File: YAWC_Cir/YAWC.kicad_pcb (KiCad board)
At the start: 2 copper layers, 65 x 36.4 mm, 30 parts, among them P1 JST-PH_2, P2 Btns, P3 CONN_5, P4 CONN_5, P5 CONN_6, U1 TPS769XX, U2 SAMD20J18A-M, U3 MMA845Q

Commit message: Mount holes
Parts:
- added X: SolderWirePad_single_2mmDrill, Wire_Pads:SolderWirePad_single_2mmDrill, F.Cu at (128.0, 95.2)
- added X: SolderWirePad_single_2mmDrill, Wire_Pads:SolderWirePad_single_2mmDrill, F.Cu at (150.6, 113.4)
- added X: SolderWirePad_single_2mmDrill, Wire_Pads:SolderWirePad_single_2mmDrill, F.Cu at (182.9, 92.2)
- moved R2 2.20 mm to (177.9, 92.0)
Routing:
- net VCC: track 195.9 -> 193.2 mm
- net SDA: track 38.6 -> 36.3 mm

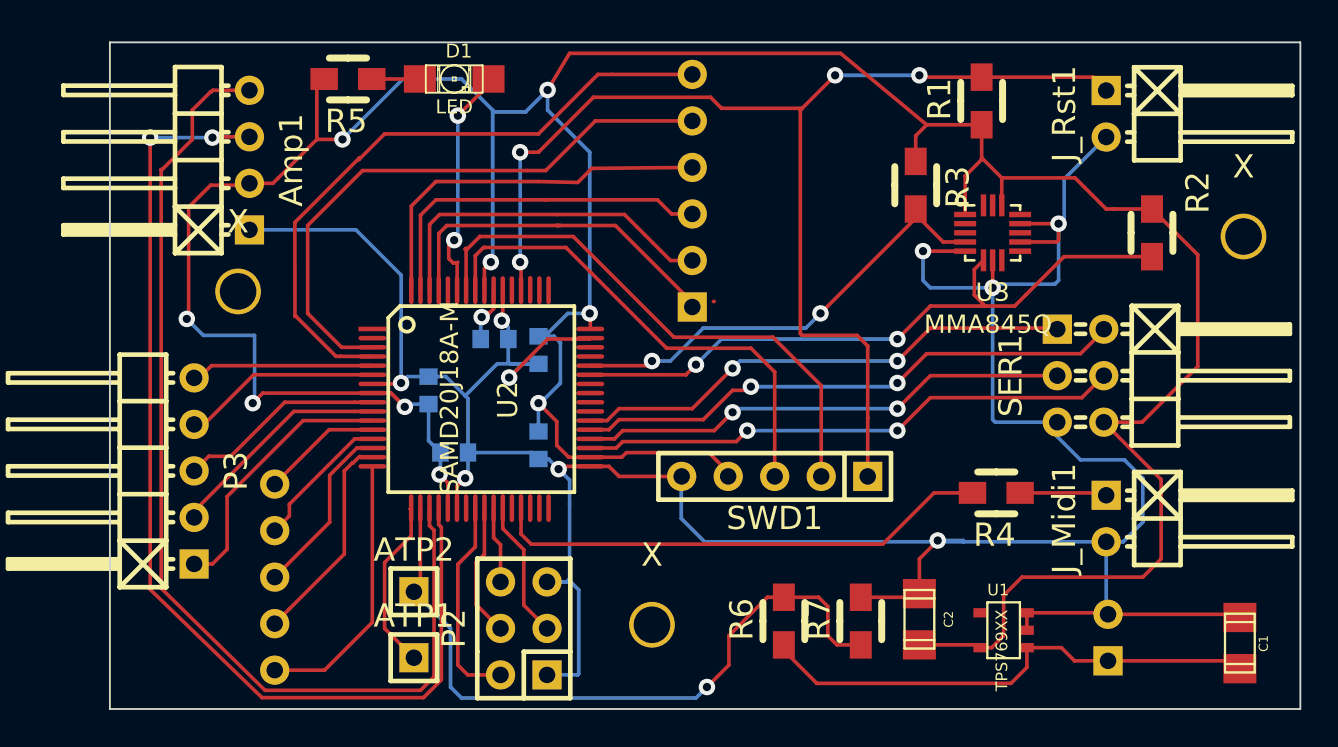
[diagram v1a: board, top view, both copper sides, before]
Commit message: Added fill Still need silk screen
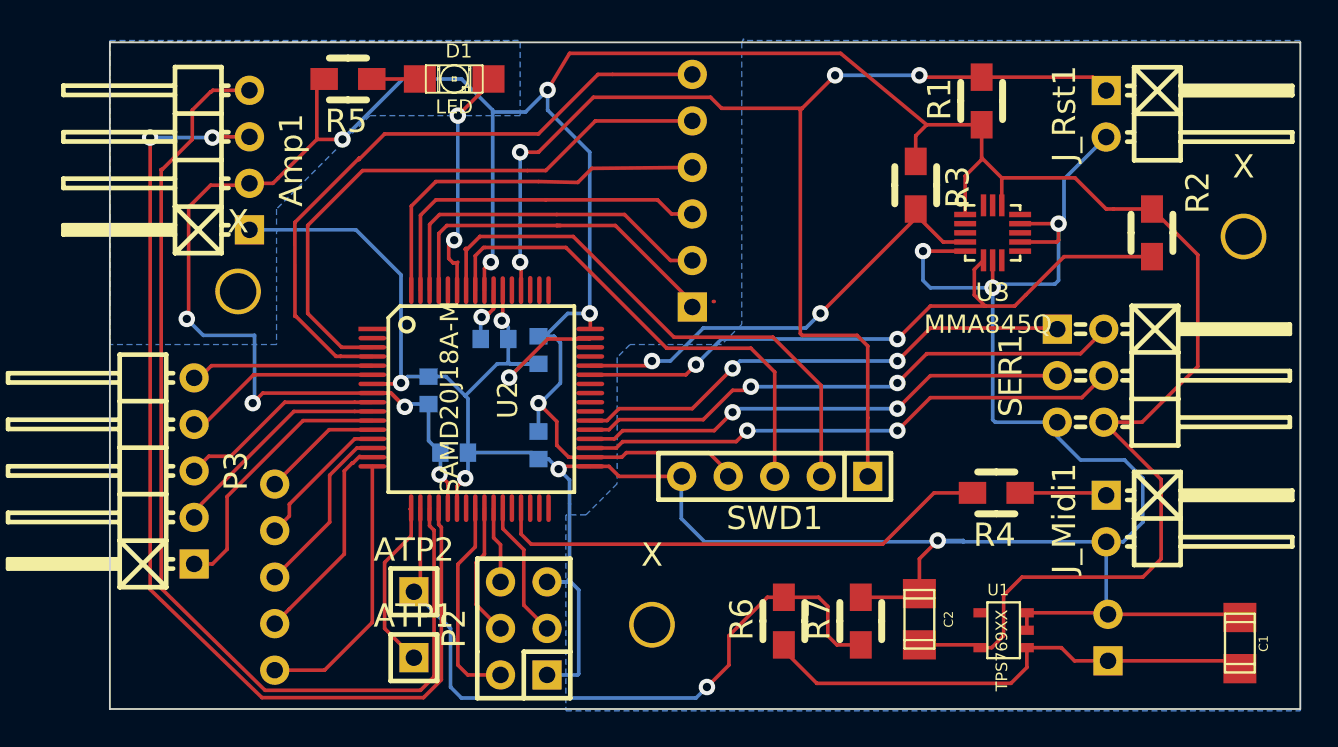
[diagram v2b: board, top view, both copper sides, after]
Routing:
- added copper zone on B.Cu, net GND

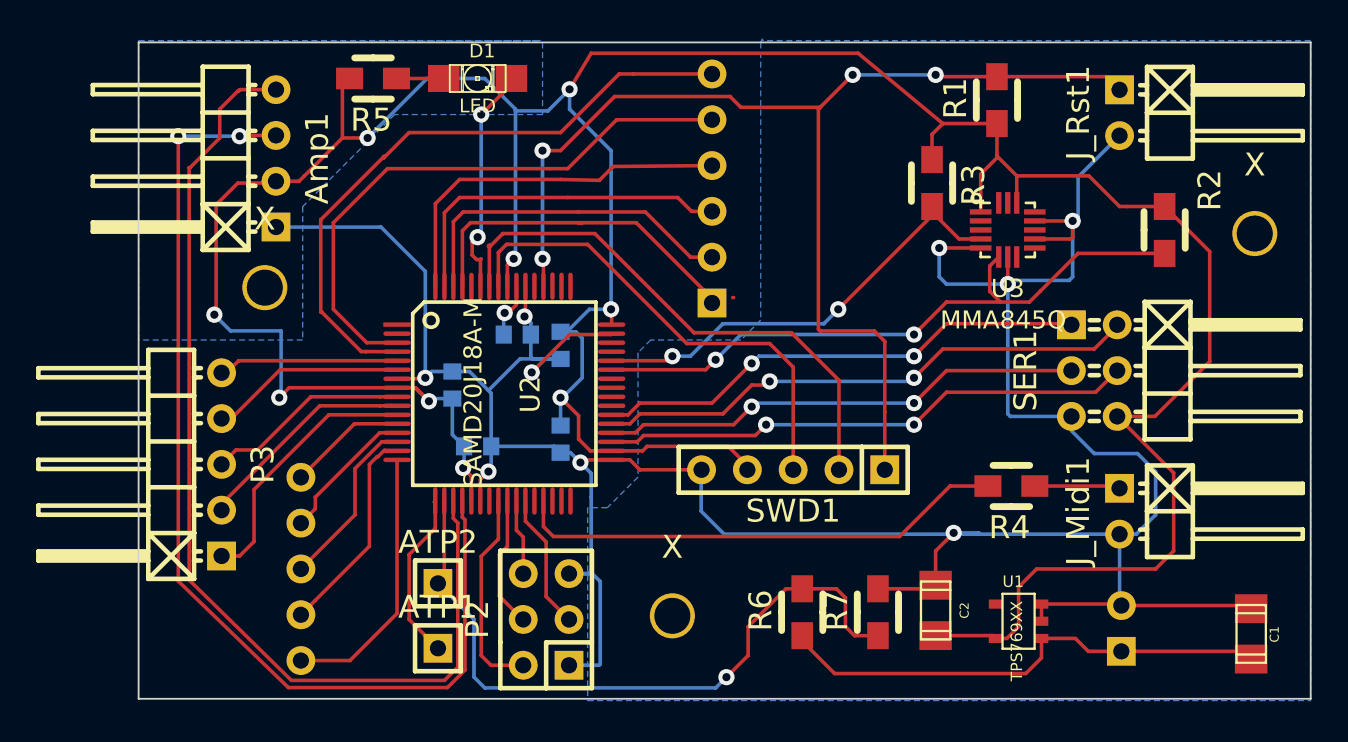
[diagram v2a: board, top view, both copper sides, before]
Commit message: Silk screen finished. Although missed polarisation off power
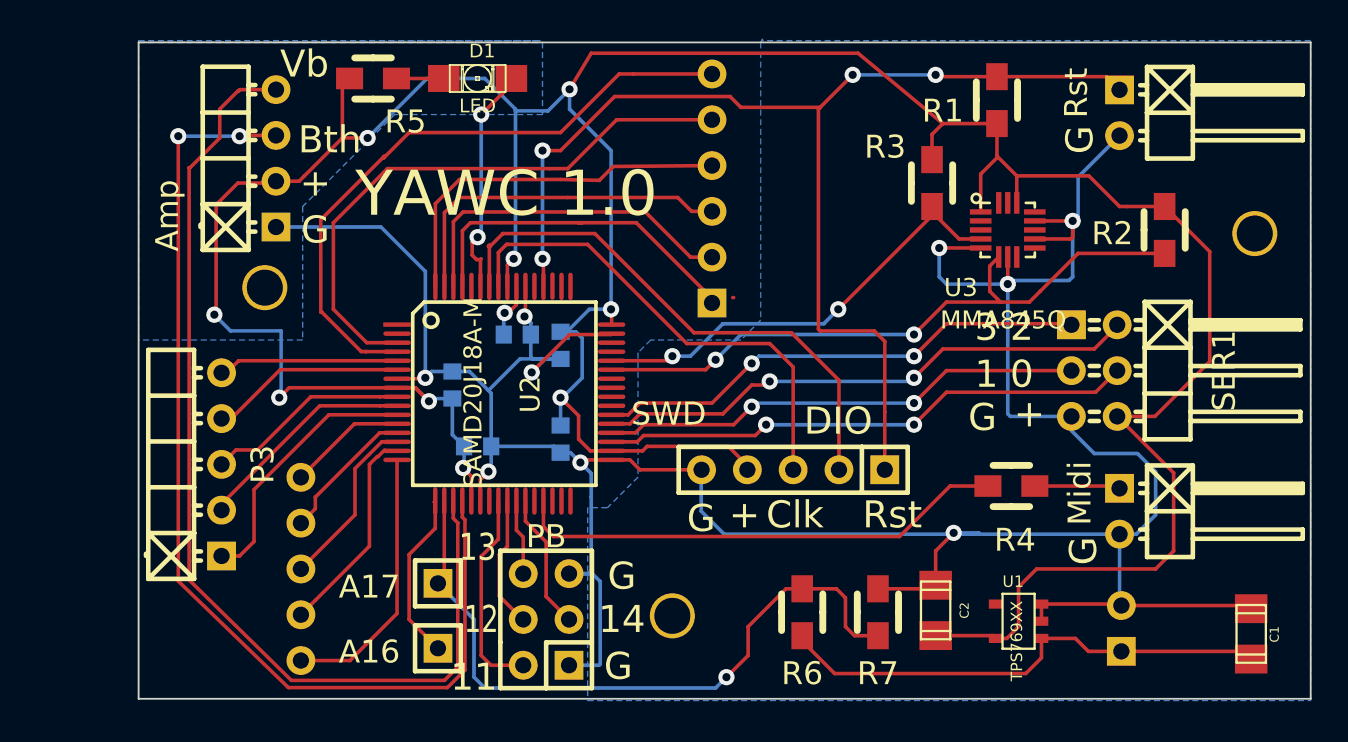
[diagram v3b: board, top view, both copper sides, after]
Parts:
-  : renamed from X
- renumbered X to ?, ATP1 to A16, ATP2 to A17, Amp1 to Amp, J_Midi1 to Midi, P2 to PB, J_Rst1 to Rst, SWD1 to SWD
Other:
- board text added: "+"
- board text added: "1 0"
- board text added: "11"
- board text added: "12"
- board text added: "13"
- board text added: "14"
- board text added: "3 2"
- board text added: "Bth"
- board text added: "Clk"
- board text added: "DIO"
- board text added: "G"
- board text added: "Rst"
- board text added: "Vb"
- board text added: "YAWC 1.0"

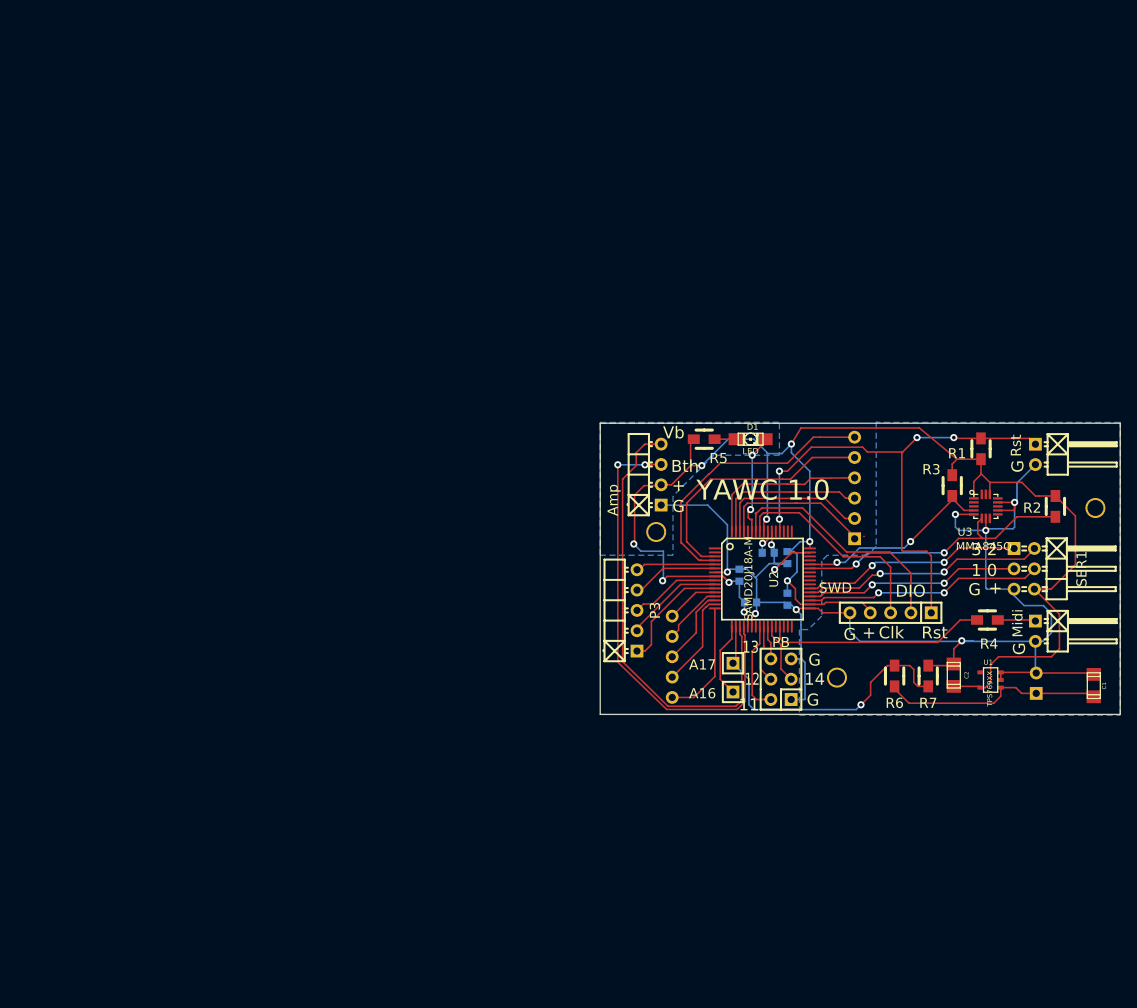
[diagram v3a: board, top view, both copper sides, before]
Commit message: More added and PCB layout of main board moved on a bit
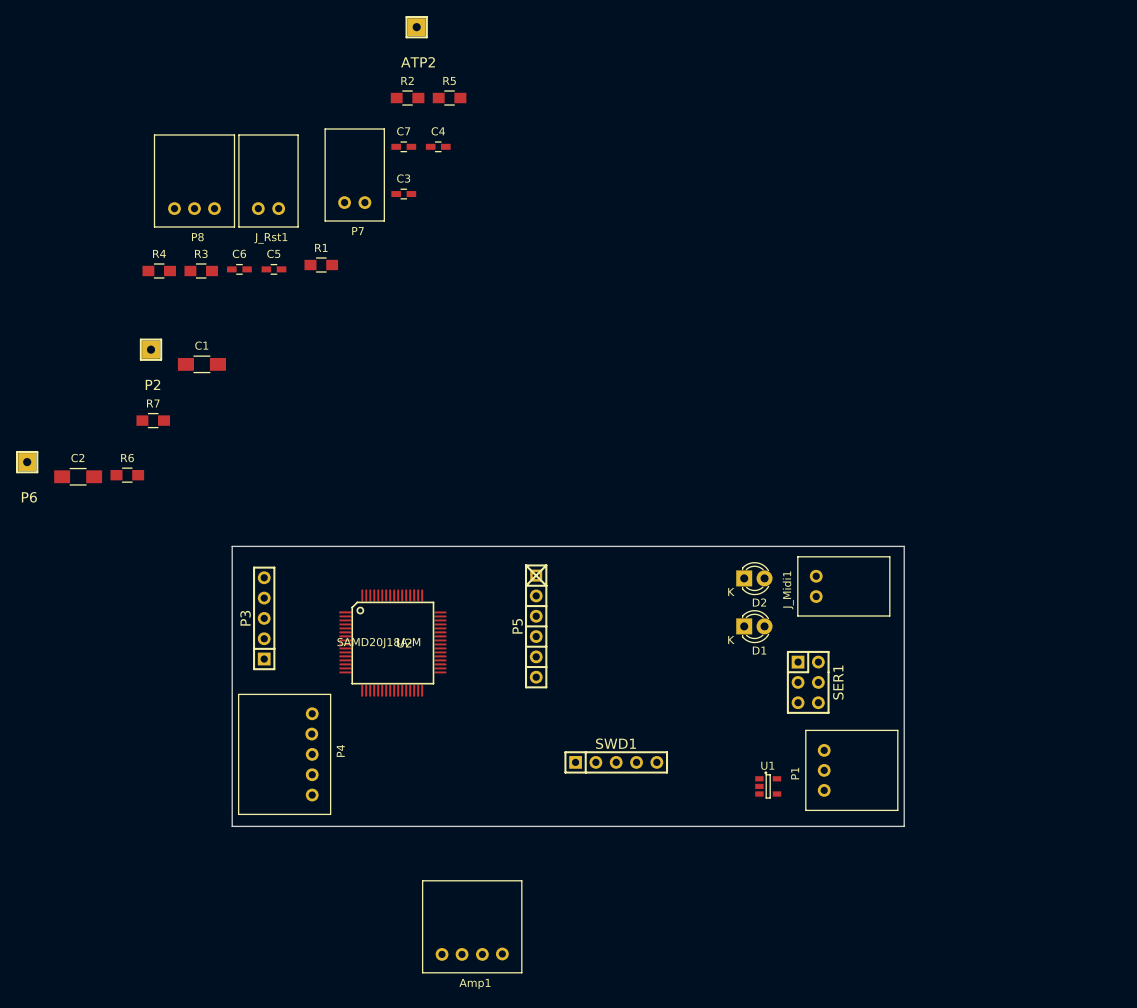
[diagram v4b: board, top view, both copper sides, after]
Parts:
- removed  : SolderWirePad_single_2mmDrill, Wire_Pads:SolderWirePad_single_2mmDrill
- removed ? (x2): SolderWirePad_single_2mmDrill, Wire_Pads:SolderWirePad_single_2mmDrill
- removed A16, A17: CONN_1, PIN_Hrd:Pin_Header_Straight_1x01
- removed Amp: CONN_4, PIN_Hdr:Pin_Header_Angled_1x04
- removed Midi, Rst: CONN_2, PIN_Hrd:Pin_Header_Angled_1x02
- removed PB: Btns, PIN_Hrd:Pin_Header_Straight_2x03
- removed SWD: CONN_5, PIN_Hdr:Pin_Header_Straight_1x05
- removed U3: MMA845Q, SMD:QFN16
- added ATP2: CONN_1, PIN_Hdr:Pin_Header_Straight_1x01, F.Cu at (98.1, 32.1)
- added Amp1: CONN_4, JST:S4B-XH, F.Cu at (105.0, 148.0)
- added D2: LED, LEDs:LED-3MM, F.Cu at (139.0, 101.0)
- added J_Midi1: CONN_2, JST:S2B-XH, F.Cu at (148.0, 102.0)
- added J_Rst1: J_Reset, JST:S2B-XH, F.Cu at (79.5, 54.8)
- added P2: TP1a, PIN_Hdr:Pin_Header_Straight_1x01, F.Cu at (64.8, 72.4)
- added P6: TP1b, PIN_Hdr:Pin_Header_Straight_1x01, F.Cu at (49.4, 86.5)
- added P7: J_AllOff, JST:S2B-XH, F.Cu at (90.3, 54.0)
- added P8: J_Pot, JST:S3B-XH, F.Cu at (70.3, 54.8)
- added SWD1: CONN_5, PIN_Hdr:Pin_Header_Straight_1x05, F.Cu at (123.0, 124.0)
- C1, C2: footprint Capacitors_SMD:c_1206 -> Capacitors_SMD:C_1206_HandSoldering
- C3, C4, C5, C6, C7: footprint Capacitors_SMD:c_0603 -> Capacitors_SMD:C_0603_HandSoldering; moved to F.Cu
- D1: footprint SMD:LED-1206 -> LEDs:LED-3MM
- P1: value JST-PH_2 -> CONN_01X03; footprint PIN_Hdr:Pin_Header_Angled_1x02 -> JST:S3B-XH; moved to F.Cu
- P3: footprint PIN_Hrd:Pin_Header_Angled_1x05 -> PIN_Hdr:Pin_Header_Straight_1x05
- P4: footprint PIN_Hrd:Pin_Header_Angled_1x05 -> JST:S5B-XH; moved to F.Cu
- P5: footprint PIN_Hrd:Pin_Header_Angled_1x06 -> PIN_Hdr:Pin_Header_1x06; moved to F.Cu
- R1, R4, R5, R6, R7: footprint Resistors_SMD:Resistor_SMD0805_HandSoldering -> Resistors_SMD:R_0805_HandSoldering
- R2: value 4k7 -> R; footprint Resistors_SMD:Resistor_SMD0805_HandSoldering -> Resistors_SMD:R_0805_HandSoldering
- R3: value 4k7 -> 10k; footprint Resistors_SMD:Resistor_SMD0805_HandSoldering -> Resistors_SMD:R_0805_HandSoldering
- SER1: footprint PIN_Hrd:Pin_Header_Angled_2x03 -> PIN_Hdr:Pin_Header_Straight_2x03
- U1: footprint SMD_Packages:SOT23-5 -> TO_SOT_Packages_SMD:SOT-23-5
- U2: footprint SMD_Packages:TQFP_64 -> SMD:TQFP_64
- moved C1 118.5 mm to (71.2, 74.2), turned to 0 degrees
- moved R4 112.3 mm to (65.9, 62.6), turned to 0 degrees
- moved C2 112.2 mm to (55.7, 88.3), turned to 0 degrees
- moved R7 102.0 mm to (65.1, 81.3), turned to 0 degrees
- moved R6 99.1 mm to (61.9, 88.1), turned to 0 degrees
- moved R3 97.6 mm to (71.1, 62.6), turned to 0 degrees
- moved R2 95.7 mm to (96.9, 41.0), turned to 0 degrees
- moved R1 85.6 mm to (86.1, 61.8), turned to 0 degrees
- moved C6 76.3 mm to (75.9, 62.4), turned to 0 degrees
- moved C5 73.6 mm to (80.2, 62.4), turned to 0 degrees
- moved C3 69.7 mm to (96.4, 53.0), turned to 0 degrees
- moved C7 68.2 mm to (96.4, 47.1), turned to 0 degrees
- moved C4 65.5 mm to (100.8, 47.1), turned to 0 degrees
- moved R5 53.2 mm to (102.2, 41.0), turned to 0 degrees
- moved U2 46.9 mm to (95.0, 109.0)
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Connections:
- C1 pad 1: /Vbatt -> GND
- P1 pad 1: /Vbatt -> GND
- P1 pad 2: GND -> VCC
- R2 pad 1: VCC -> Net-(D2-Pad2)
- R2 pad 2: SDA -> VCC
- R3 pad 2: SCL -> Net-(P8-Pad1)
- R6 pad 1: /Vbatt -> GND
- U1 pad 1: /Vbatt -> GND
- U2 pad 24: /Micro/PB11 -> Net-(P7-Pad1)
- U2 pad 25: /Micro/PB12 -> (no net)
- U2 pad 26: /Micro/PB13 -> (no net)
- U2 pad 27: /Micro/PB14 -> (no net)
- U2 pad 43: SDA -> (no net)
- U2 pad 44: SCL -> (no net)
- U2 pad 60: (no net) -> Net-(D2-Pad1)
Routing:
- net VCC: track 193.2 -> 0.00 mm, vias 9 -> 0
- net GND: track 173.3 -> 0.00 mm, vias 9 -> 0
- net /Micro/Reset: track 65.6 -> 0.00 mm, vias 4 -> 0
- net Bth: track 58.3 -> 0.00 mm, vias 2 -> 0
- net Vib: track 57.2 -> 0.00 mm
- net BatSample: track 38.6 -> 0.00 mm, vias 1 -> 0
- net SDA: track 36.3 -> 0.00 mm, vias 2 -> 0
- net /Micro/Y1: track 35.5 -> 0.00 mm
- net /Micro/Y0: track 32.5 -> 0.00 mm
- net /Micro/SWDIO: track 30.4 -> 0.00 mm
- net /Micro/S1P2: track 30.4 -> 0.00 mm, vias 2 -> 0
- net /Micro/S1P0: track 29.7 -> 0.00 mm, vias 2 -> 0
- net /Vbatt: track 27.9 -> 0.00 mm
- net /Micro/S1P3: track 27.6 -> 0.00 mm, vias 2 -> 0
- net /Micro/Tx: track 27.5 -> 0.00 mm
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- removed copper zone on B.Cu, net GND
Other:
- board size 65 x 36.4 mm -> 84 x 35 mm
- net class Default: trace_width 0.2 -> 0.25; via_dia 0.9 -> 0.6; via_drill 0.5 -> 0.4
- net class Min removed
- rule trace_min: 0.16 -> 0.2
- rule via_min_drill: 0.326 -> 0.3
- rule via_min_size: 0.7 -> 0.4
- board text removed: "+"
- board text removed: "1 0"
- board text removed: "11"
- board text removed: "12"
- board text removed: "13"
- board text removed: "14"
- board text removed: "3 2"
- board text removed: "Bth"
- board text removed: "Clk"
- board text removed: "DIO"
- board text removed: "G"
- board text removed: "Rst"
- board text removed: "Vb"
- board text removed: "YAWC 1.0"
